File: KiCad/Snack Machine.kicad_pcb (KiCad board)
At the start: 2 copper layers, 76 x 106 mm, 110 parts, among them J1 RFID_CONNECTOR, J10 Row Screw Terminal, J11 Column Screw Terminal, J12 Display Serial Header, J17 AVR-ISP-6, J2 Power Screw Terminal, J3 USB_C_Receptacle_USB2.0, J4 V2 Display Ribbon Cable, J5 MDB, J6 Conn_01x02, J7 LCD EXP1, J8 LCD EXP2, J9 AVR-ISP-6, Q1 P-CH 30V 3.8A, Q2 MMBT3904, Q3 MMBT3904, SW1 SW_SPST, U1 DPS1133FIA-13, U2 MEZD71202A-G, U3 ATmega2560-16AU, U4 TBD62783A, U5 Huzzah32, U6 ATmega16U2-MU, U7 SN74LVC1T45DBV, U8 SN74LVC1T45DBV, Y1 16MHz, Y2 16MHz

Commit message: Sourcing parts
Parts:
- C2: value 22 uF -> 22uF
- C21, C6: value 100 nF -> 100nF
- C22, C4: value 2.2 uF -> 2.2uF
- C8: value 1 nF -> 1nF
- J1: footprint Connector_PinHeader_2.54mm:PinHeader_1x10_P2.54mm_Vertical -> Snack Machine:CONN_HEADER_VERT_10POS_2.54MM
- J6: footprint Connector_PinHeader_2.54mm:PinHeader_1x02_P2.54mm_Vertical -> Snack Machine:CONN_HEADER_VERT_2POS_2.54MM
- R11: renamed from R25; value 5.1 k -> 5k1
- R17, R19, R2, R20, R21, R22, R31, R8, R9: value 1 k -> 1k
- R18: value 330 k -> 330k
- R23: value 270 k -> 270k
- R24: value 100 k -> 100k
- R25: renamed from R26; value 5.1 k -> 5k1
- Y1, Y2: footprint Crystal:Resonator_SMD_muRata_CSTxExxV-3Pin_3.0x1.1mm_HandSoldering -> Snack Machine:Resonator_SMD_ECS-CR2-16.00-B-TR
- moved R3 3.50 mm to (158.2, 112.1)
- moved J6 2.75 mm to (162.9, 111.4)
- moved Y2 0.71 mm to (158.4, 58.8)
- moved Y1 0.28 mm to (124.8, 101.3)
- renumbered C25 to C17, C26 to C18, C27 to C19, C29 to C20, C30 to C23, C23 to C7, C24 to C9, J17 to J13, R55 to R26, R56 to R32, R57 to R33, R58 to R34, R59 to R35, R60 to R36, R61 to R37, R62 to R38, R63 to R39
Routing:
- net GND: track 118.0 -> 159.7 mm, vias 25 -> 45
- net +5V: track 284.2 -> 291.1 mm, vias 17 -> 16
- net (no net): track 0.00 -> 5.94 mm, vias 0 -> 2
- net /MISO: track 100.0 -> 101.7 mm
- net /DOOR_SW: track 24.6 -> 23.4 mm
- net /MOSI: track 90.2 -> 91.3 mm
- net /SCK: track 97.1 -> 98.2 mm
- net Net-(C17-Pad2): track 7.92 -> 8.76 mm
- net Net-(C7-Pad2): track 8.06 -> 8.90 mm
- net /TX_HUZZAH_MEGA: track 48.0 -> 47.5 mm
- added copper zone on F.Cu, net GND
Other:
- board text added: "+"
- board text added: "+5V"
- board text added: "Beep"
- board text added: "Dat0"
- board text added: "Dat1"
- board text added: "EXP1"
- board text added: "EXP2"
- board text added: "GND"
- board text added: "Green"
- board text added: "NC"
- board text added: "Red"

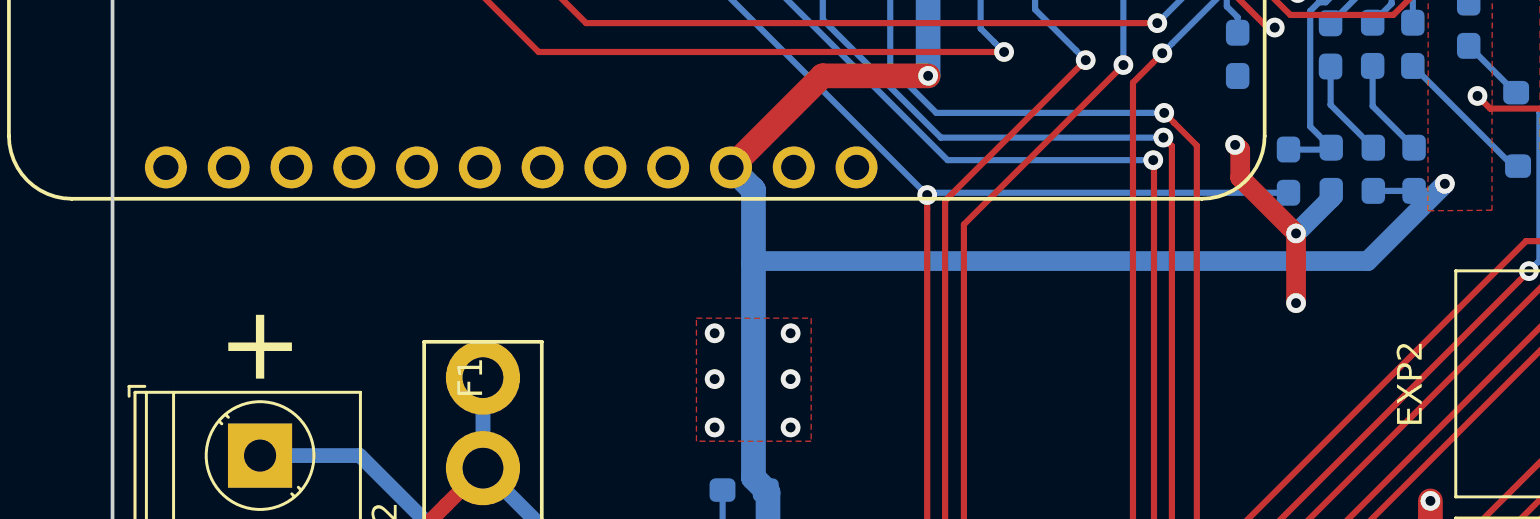
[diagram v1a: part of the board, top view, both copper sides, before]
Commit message: Adding source to SilkScreen
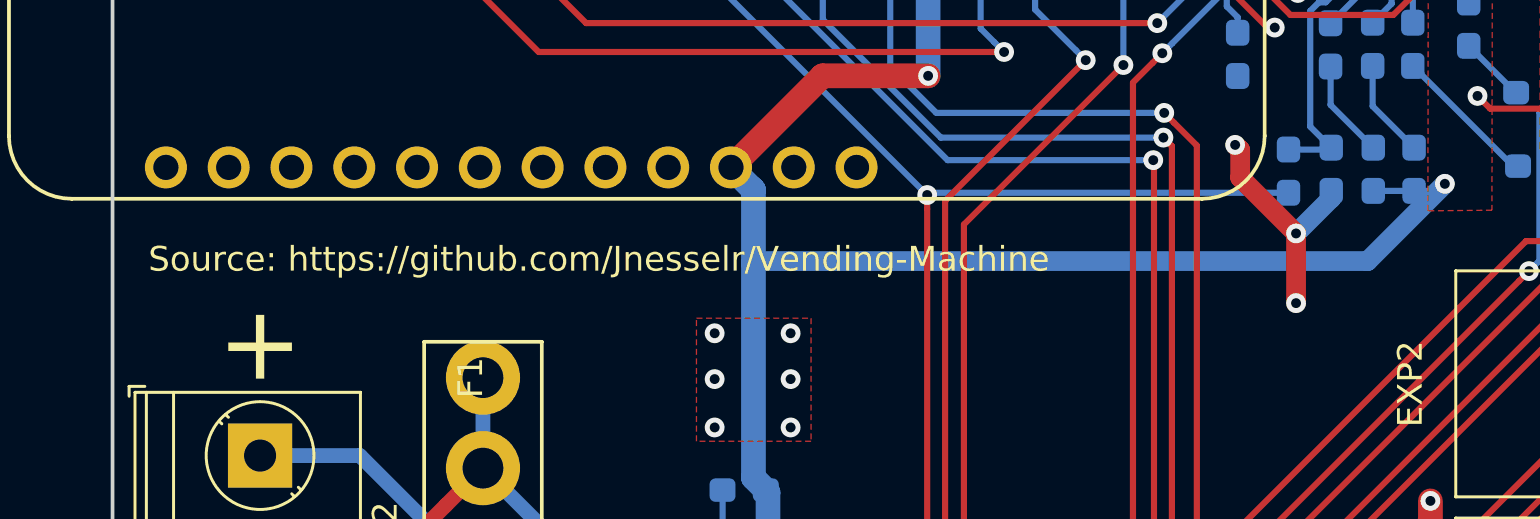
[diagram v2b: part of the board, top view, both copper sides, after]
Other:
- board text added: "Source: https://github.com/Jnesselr/Vending-Machine"
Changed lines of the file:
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@@
   (general
     (thickness 1.6)
-    (drawings 23)
+    (drawings 24)
     (tracks 1262)
     (zones 0)
@@
     (add_net /RESET_HUZZAH)
     (add_net /RFID_BEEP_CTRL)
-    (add_net /RFID_CARD_PRESENT)
     (add_net /RFID_DATA_0)
     (add_net /RFID_DATA_1)
     (add_net /RFID_GREEN_LED)
-    (add_net /RFID_HOLD)
     (add_net /RFID_RED_LED)
     (add_net /RX_DISPLAY_MEGA)
@@
     (add_net "Net-(D6-Pad2)")
     (add_net "Net-(D9-Pad3)")
-    (add_net "Net-(J12-Pad10)")
-    (add_net "Net-(J12-Pad2)")
-    (add_net "Net-(J12-Pad4)")
-    (add_net "Net-(J12-Pad6)")
-    (add_net "Net-(J12-Pad8)")
     (add_net "Net-(J3-PadA5)")
-    (add_net "Net-(J3-PadA8)")
     (add_net "Net-(J3-PadB5)")
-    (add_net "Net-(J3-PadB8)")
-    (add_net "Net-(J4-Pad10)")
-    (add_net "Net-(J4-Pad11)")
-    (add_net "Net-(J4-Pad12)")
-    (add_net "Net-(J4-Pad13)")
-    (add_net "Net-(J4-Pad14)")
-    (add_net "Net-(J4-Pad15)")
-    (add_net "Net-(J4-Pad16)")
-    (add_net "Net-(J4-Pad17)")
-    (add_net "Net-(J4-Pad18)")
-    (add_net "Net-(J4-Pad19)")
-    (add_net "Net-(J4-Pad2)")
-    (add_net "Net-(J4-Pad20)")
-    (add_net "Net-(J4-Pad28)")
-    (add_net "Net-(J4-Pad29)")
-    (add_net "Net-(J4-Pad3)")
-    (add_net "Net-(J4-Pad4)")
-    (add_net "Net-(J4-Pad5)")
-    (add_net "Net-(J4-Pad6)")
-    (add_net "Net-(J4-Pad7)")
-    (add_net "Net-(J4-Pad8)")
-    (add_net "Net-(J4-Pad9)")
-    (add_net "Net-(J5-Pad3)")
     (add_net "Net-(J5-Pad5)")
-    (add_net "Net-(J8-Pad10)")
-    (add_net "Net-(J8-Pad9)")
     (add_net "Net-(Q2-Pad1)")
     (add_net "Net-(Q2-Pad3)")
@@
     (add_net "Net-(R23-Pad1)")
     (add_net "Net-(R7-Pad2)")
-    (add_net "Net-(U3-Pad1)")
-    (add_net "Net-(U3-Pad15)")
-    (add_net "Net-(U3-Pad16)")
-    (add_net "Net-(U3-Pad17)")
-    (add_net "Net-(U3-Pad19)")
-    (add_net "Net-(U3-Pad23)")
-    (add_net "Net-(U3-Pad24)")
-    (add_net "Net-(U3-Pad25)")
-    (add_net "Net-(U3-Pad26)")
-    (add_net "Net-(U3-Pad27)")
-    (add_net "Net-(U3-Pad28)")
-    (add_net "Net-(U3-Pad29)")
-    (add_net "Net-(U3-Pad4)")
-    (add_net "Net-(U3-Pad47)")
-    (add_net "Net-(U3-Pad48)")
-    (add_net "Net-(U3-Pad49)")
-    (add_net "Net-(U3-Pad5)")
-    (add_net "Net-(U3-Pad50)")
-    (add_net "Net-(U3-Pad51)")
-    (add_net "Net-(U3-Pad52)")
-    (add_net "Net-(U3-Pad65)")
-    (add_net "Net-(U3-Pad66)")
-    (add_net "Net-(U3-Pad70)")
-    (add_net "Net-(U3-Pad71)")
-    (add_net "Net-(U3-Pad72)")
-    (add_net "Net-(U3-Pad73)")
-    (add_net "Net-(U3-Pad74)")
-    (add_net "Net-(U3-Pad75)")
-    (add_net "Net-(U3-Pad76)")
-    (add_net "Net-(U3-Pad77)")
-    (add_net "Net-(U3-Pad79)")
-    (add_net "Net-(U3-Pad82)")
-    (add_net "Net-(U3-Pad83)")
-    (add_net "Net-(U3-Pad84)")
-    (add_net "Net-(U3-Pad85)")
-    (add_net "Net-(U5-Pad1)")
-    (add_net "Net-(U5-Pad10)")
-    (add_net "Net-(U5-Pad11)")
-    (add_net "Net-(U5-Pad12)")
-    (add_net "Net-(U5-Pad13)")
     (add_net "Net-(U5-Pad14)")
     (add_net "Net-(U5-Pad15)")
-    (add_net "Net-(U5-Pad16)")
-    (add_net "Net-(U5-Pad17)")
-    (add_net "Net-(U5-Pad18)")
-    (add_net "Net-(U5-Pad19)")
-    (add_net "Net-(U5-Pad2)")
-    (add_net "Net-(U5-Pad20)")
-    (add_net "Net-(U5-Pad21)")
-    (add_net "Net-(U5-Pad22)")
-    (add_net "Net-(U5-Pad23)")
-    (add_net "Net-(U5-Pad24)")
-    (add_net "Net-(U5-Pad26)")
-    (add_net "Net-(U5-Pad4)")
-    (add_net "Net-(U5-Pad5)")
-    (add_net "Net-(U5-Pad6)")
-    (add_net "Net-(U5-Pad7)")
-    (add_net "Net-(U5-Pad8)")
-    (add_net "Net-(U5-Pad9)")
-    (add_net "Net-(U6-Pad12)")
-    (add_net "Net-(U6-Pad14)")
-    (add_net "Net-(U6-Pad18)")
-    (add_net "Net-(U6-Pad19)")
-    (add_net "Net-(U6-Pad20)")
-    (add_net "Net-(U6-Pad21)")
-    (add_net "Net-(U6-Pad22)")
-    (add_net "Net-(U6-Pad23)")
-    (add_net "Net-(U6-Pad25)")
-    (add_net "Net-(U6-Pad26)")
-    (add_net "Net-(U6-Pad5)")
-    (add_net "Net-(U6-Pad6)")
-    (add_net "Net-(U6-Pad7)")
   )
   (net_class "High Amp" ""
@@
     )
   )
+  (gr_text "Source: https://github.com/Jnesselr/Vending-Machine" (at 101.4476 74.9554) (layer F.SilkS)
+    (effects (font (size 1 1) (thickness 0.15)) (justify left))
+  )
   (gr_text EXP2 (at 152.5 80 90) (layer F.SilkS)

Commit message: Fixing some small issues here and there
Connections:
- net /USB_Serial/MICRO_RX renamed Net-(R36-Pad2)
- net /USB_Serial/MICRO_TX renamed Net-(R35-Pad2)
- R15 pad 1: /USB_Serial/RX_USB -> /USB_Serial/TX_USB
- R16 pad 1: /USB_Serial/TX_USB -> /USB_Serial/RX_USB
- R35 pad 1: /USB_Serial/TX_USB -> /USB_Serial/RX_USB
- R36 pad 1: /USB_Serial/RX_USB -> /USB_Serial/TX_USB
- U3 pad 78: /MOTOR_CURRENT -> (no net)
- U3 pad 85: (no net) -> /MOTOR_CURRENT
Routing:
- net (no net): track 5.94 -> 0.00 mm, vias 2 -> 0
- net GND: track 159.7 -> 165.7 mm, vias 45 -> 47
- net /USB_Serial/TX_USB: track 2.70 -> 5.93 mm
- net /USB_Serial/RX_USB: track 5.93 -> 2.70 mm
- net /MOTOR_CURRENT: track 34.4 -> 35.8 mm

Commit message: Making some board modifications for the final revision
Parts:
- removed C2: 22uF, Capacitor_SMD:C_1210_3225Metric_Pad1.42x2.65mm_HandSolder
- removed C21, C6: 100nF, Capacitor_SMD:C_0603_1608Metric_Pad1.05x0.95mm_HandSolder
- removed C22, C4: 2.2uF, Capacitor_SMD:C_0603_1608Metric_Pad1.05x0.95mm_HandSolder
- removed C8: 1nF, Capacitor_SMD:C_0603_1608Metric_Pad1.05x0.95mm_HandSolder
- removed U1: DPS1133FIA-13, Snack Machine:DPS1133FIA-13
- added Q4: MMBT3904, Snack Machine:SOT-23_Handsoldering_Lite, B.Cu at (124.5, 106.0)
- added Q5: P-CH 30V 3.8A, Snack Machine:SOT-23_Handsoldering_Lite, B.Cu at (118.1, 106.7)
- added R40: 47k, Resistor_SMD:R_0603_1608Metric_Pad1.05x0.95mm_HandSolder, B.Cu at (125.1, 113.0)
- added R41: 10k, Resistor_SMD:R_0603_1608Metric_Pad1.05x0.95mm_HandSolder, B.Cu at (129.8, 113.0)
- R18: value 330k -> 1k
- R23: value 270k -> 10k
- R24: value 100k -> 10k
- R31: value 1k -> 4.7k; moved to B.Cu
- moved R18 13.6 mm to (128.9, 105.4), turned to 0 degrees
- moved R23 9.07 mm to (118.7, 102.2), turned to 0 degrees
- moved R24 8.05 mm to (114.9, 106.7), turned to 270 degrees
- moved R31 2.77 mm to (128.3, 109.2), turned to 0 degrees
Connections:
- D15 pad 2: Net-(C22-Pad1) -> Net-(D15-Pad2)
- R18 pad 2: GND -> /MOTORS_ENABLE
- R23 pad 1: Net-(R23-Pad1) -> +24V
- R23 pad 2: GND -> Net-(Q4-Pad3)
- R24 pad 1: /MOTOR_CURRENT -> Net-(D15-Pad2)
- R24 pad 2: GND -> +24V
- R31 pad 1: +5V -> Net-(Q4-Pad2)
- R31 pad 2: /MOTOR_FAULT -> GND
- U3 pad 12: /TX_DISPLAY_MEGA -> /RX_DISPLAY_MEGA
- U3 pad 13: /RX_DISPLAY_MEGA -> /TX_DISPLAY_MEGA
- U3 pad 43: /MOTOR_FAULT -> (no net)
- U3 pad 63: /TX_MDB_MEGA -> /RX_MDB_MEGA
- U3 pad 64: /RX_MDB_MEGA -> /TX_MDB_MEGA
- U3 pad 85: /MOTOR_CURRENT -> /MOTOR_SENSE
- U4 pad 9: Net-(C22-Pad1) -> Net-(D15-Pad2)
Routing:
- net /MOTOR_CURRENT: track 35.8 -> 0.00 mm, vias 1 -> 0
- net Net-(D15-Pad2): track 0.00 -> 33.2 mm
- net /MOTOR_SENSE: track 0.00 -> 25.5 mm, vias 0 -> 1
- net Net-(C22-Pad1): track 25.0 -> 0.00 mm
- net /MOTORS_ENABLE: track 24.5 -> 4.65 mm, vias 3 -> 1
- net /MOTOR_FAULT: track 19.7 -> 0.00 mm, vias 1 -> 0
- net +24V: track 144.1 -> 156.4 mm
- net Net-(Q4-Pad3): track 0.00 -> 9.65 mm
- net Net-(R23-Pad1): track 7.70 -> 0.00 mm
- net +5V: track 291.1 -> 286.4 mm
- net Net-(C8-Pad1): track 4.69 -> 0.00 mm
- net Net-(C6-Pad1): track 4.64 -> 0.00 mm
- net Net-(Q4-Pad1): track 5.69 -> 2.45 mm
- net Net-(Q4-Pad2): track 0.00 -> 2.92 mm
- net GND: track 165.7 -> 167.8 mm, vias 47 -> 48

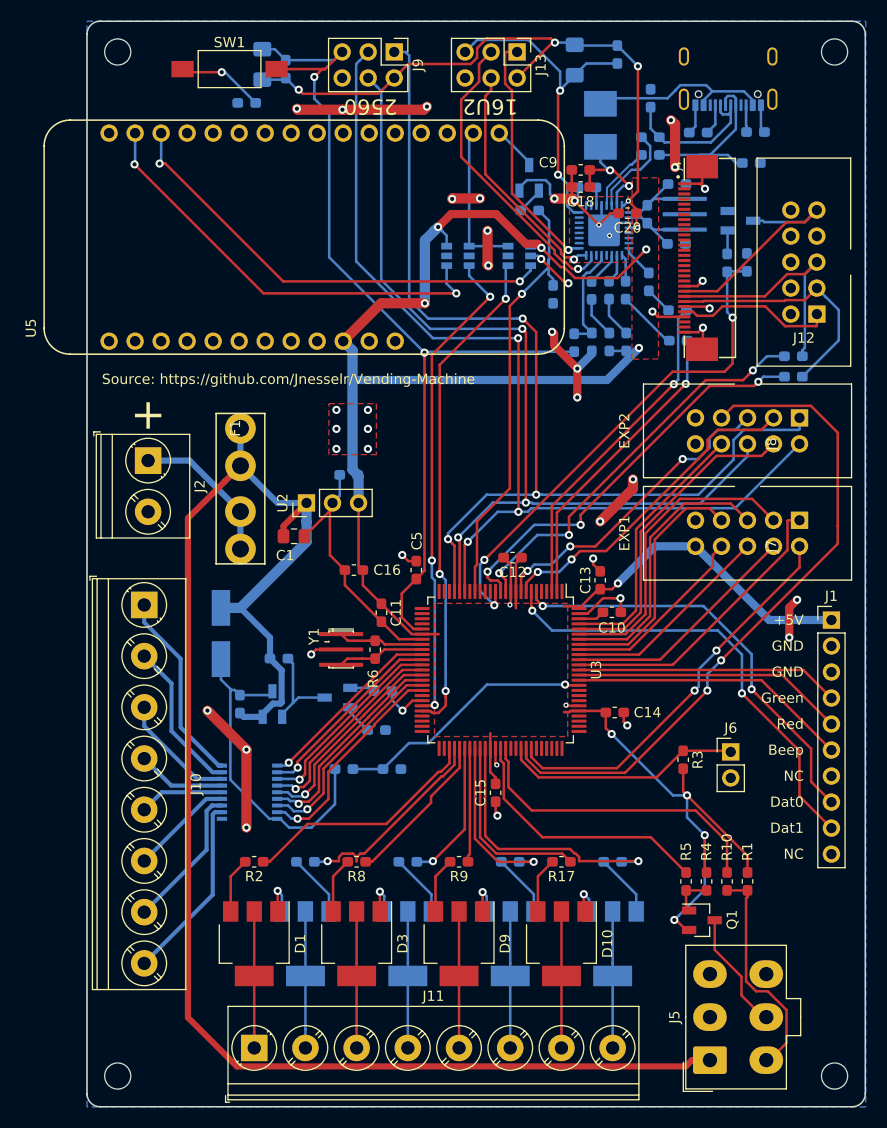
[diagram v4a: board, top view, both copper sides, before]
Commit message: Updating board to remove EXP1/EXP2
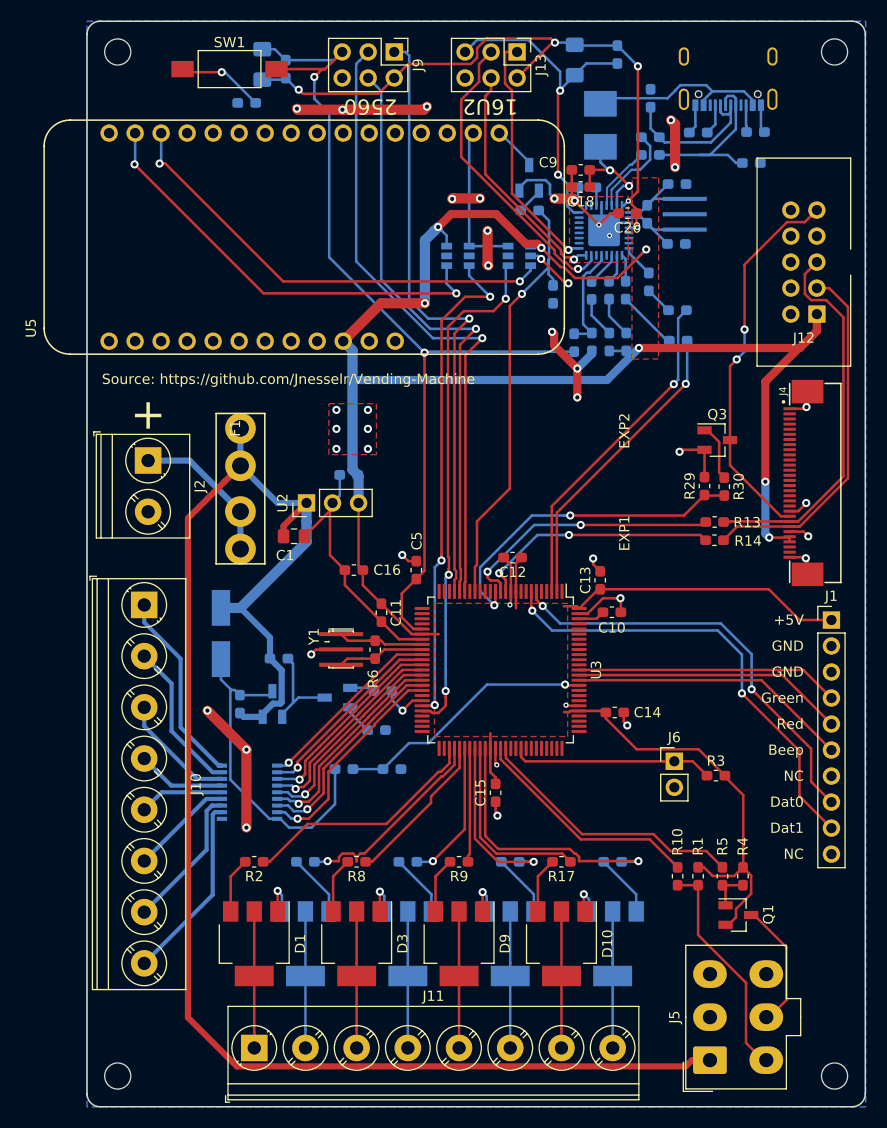
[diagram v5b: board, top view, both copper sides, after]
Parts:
- removed J7: LCD EXP1, Snack Machine:PinHeader_2x05_P2.54mm_Vertical
- removed J8: LCD EXP2, Snack Machine:PinHeader_2x05_P2.54mm_Vertical
- Q3, R13, R14, R29, R30: moved to F.Cu
- moved J4 24.3 mm to (170.8, 85.1)
- moved R29 22.2 mm to (160.3, 85.4)
- moved R30 21.8 mm to (162.2, 85.4)
- moved Q3 21.5 mm to (161.5, 80.9)
- moved R14 19.5 mm to (161.3, 90.7)
- moved R13 16.1 mm to (161.3, 88.9)
- moved J6 5.59 mm to (157.4, 112.3)
- moved R1 4.85 mm to (159.7, 123.5)
- moved R10 4.85 mm to (157.7, 123.5)
- moved Q1 3.59 mm to (163.6, 127.3)
- moved R4 3.59 mm to (164.1, 123.5)
- moved R5 3.59 mm to (162.1, 123.5)
- moved R3 3.56 mm to (161.4, 113.7), turned to 0 degrees
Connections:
- net /RX_HUZZAH_MEGA renamed /HUZZAH_RX_MEGA_TX
- net /RX_MDB renamed /MDB_TX
- net /RX_MDB_MEGA renamed /MDB_TX_MEGA_RX
- net /TX_HUZZAH_MEGA renamed /HUZZAH_TX_MEGA_RX
- net /TX_MDB renamed /MDB_RX
- net /TX_MDB_MEGA renamed /MDB_RX_MEGA_TX
- J12 pad 3: /4D_Display/RX_DISPLAY -> /4D_Display/DISPLAY_TX
- J12 pad 5: /4D_Display/TX_DISPLAY -> /4D_Display/DISPLAY_RX
- J4 pad 23: /4D_Display/TX_DISPLAY -> /4D_Display/DISPLAY_RX
- J4 pad 24: /4D_Display/RX_DISPLAY -> /4D_Display/DISPLAY_TX
- R13 pad 1: /RX_DISPLAY_MEGA -> /DISPLAY_RX_MEGA_TX
- R13 pad 2: /4D_Display/RX_DISPLAY -> /4D_Display/DISPLAY_RX
- R14 pad 1: /TX_DISPLAY_MEGA -> /DISPLAY_TX_MEGA_RX
- R14 pad 2: /4D_Display/TX_DISPLAY -> /4D_Display/DISPLAY_TX
- U3 pad 12: /RX_DISPLAY_MEGA -> /DISPLAY_TX_MEGA_RX
- U3 pad 13: /TX_DISPLAY_MEGA -> /DISPLAY_RX_MEGA_TX
- U3 pad 68: /SD_DET -> (no net)
- U3 pad 69: /BTN_ENC -> (no net)
- U3 pad 8: /BTN_EN2 -> (no net)
- U3 pad 89: /LCD_BEEP -> (no net)
- U3 pad 9: /BTN_EN1 -> (no net)
- U3 pad 90: /LCD_CS -> (no net)
- U3 pad 91: /LCD_5 -> (no net)
- U3 pad 92: /LCD_7 -> (no net)
- U3 pad 93: /LCD_6 -> (no net)
- U3 pad 94: /LCD_4 -> (no net)
- U3 pad 95: /LCD_EN -> (no net)
- U3 pad 96: /SD_CS -> (no net)
- U3 pad 97: /LCD_RESET -> (no net)
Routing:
- net /SD_DET: track 66.0 -> 0.00 mm, vias 2 -> 0
- net /MISO: track 101.7 -> 59.5 mm, vias 3 -> 1
- net /RX_DISPLAY_MEGA: track 40.3 -> 0.00 mm, vias 3 -> 0
- net /TX_DISPLAY_MEGA: track 39.7 -> 0.00 mm, vias 3 -> 0
- net /BTN_ENC: track 38.7 -> 0.00 mm, vias 2 -> 0
- net /4D_Display/DISPLAY_RX: track 0.00 -> 37.4 mm
- net /SCK: track 98.2 -> 61.8 mm, vias 3 -> 1
- net /4D_Display/DISPLAY_TX: track 0.00 -> 35.2 mm
- net /MOSI: track 91.3 -> 57.8 mm, vias 3 -> 1
- net /BTN_EN2: track 32.2 -> 0.00 mm, vias 2 -> 0
- net /SD_CS: track 31.1 -> 0.00 mm
- net /BTN_EN1: track 30.5 -> 0.00 mm, vias 3 -> 0
- net /LCD_EN: track 30.0 -> 0.00 mm
- net /LCD_BEEP: track 29.0 -> 0.00 mm
- net /LCD_4: track 27.1 -> 0.00 mm
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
